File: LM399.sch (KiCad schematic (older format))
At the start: 8 parts, among them U1 LM399, U2 LTC2057

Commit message: Positive zener pin now has a sense connection to correct fot the error caused by the 1 mA zener current Changed zener bias current resistor to less expensive smd precision resistor Added a 2nd parallel resistor to the divider to make fine tuning easier Changed pin layout of the connector (due to the sense connection)
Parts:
- added R4: 34k, Custom_footprints:Vishay_S102K, symbol R
- added W1, W3: NET-TIE, Custom_footprints:NET-TIE-0.15mm, symbol NET-TIE
- added W2: NET-TIE, Custom_footprints:NET-TIE-0.20mm, symbol NET-TIE
- C1: Alternative (none) -> C1206C223J2GACAUTO; MFN Cornell Dubilier -> Kemet; MFP FCP1206H103J-H2 -> C1206C103JAGACTU; Note (none) -> Use *that* one!
- R1: value 3K -> 7.5K; footprint Custom_footprints:Vishay_S102 -> Resistors_SMD:R_0805; MFN Vishay -> Welwyn; MFP Y00623K00000B9L -> PCF0805-13-7K5-B-T1; Note TCR <= 5ppm, absolute precision unimportant -> (none)
- R2: value 9K -> 20k; footprint Custom_footprints:Vishay_S102 -> Custom_footprints:Vishay_S102K; MFP Y00629K00000T9L -> Y006220K0000T9L
- R3: value 20K -> 34k; footprint Custom_footprints:Vishay_S102 -> Custom_footprints:Vishay_S102K; MFP Y006220K0000T9L -> Y006234K0000T9L
- U1: MFP LM399A -> LM399AH
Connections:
- net labels added: V-heater+, V_heater-, V_zener+_force, V_zener+_sense
- wire segments 28 -> 37
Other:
- note added: "Information on insulation resistance can be found here:\nhttp://www.iequalscdvdt.com/Insulation_resis_.html\nhttps://www.vishay.com/docs/26033/gentechinfofilm.pdf"
- note added: "Kelvin connect the Zener. Even the the small current\npassing through R1 (1 mA) will introduce an error of 0.2 ppm/K\n(10 mm trace 0=> 0.2 ohm, 1 mA, 0.7 % tcr, ~~7 V reference)"
- note added: "Use a Film capacitor with a high insulation\nresistance (no polyester), which is stable\nover temperature. Nowadays C0G (BME) is\neven better than film."
- note added: "Use precision resistors\nwith an extremly low TCR\nor a network with very good\ntracking TCR."
- note added: "e.g. PCF0805-13-7K5-B-T1 (5 ppm),\nTE Connectivity RU73X2A7K5LTDF (2 ppm),\nVishay S102 (2 ppm)\n\nPCF0805-13-3K-B-T1. (5 ppm),\nVishay S102 (2 ppm)"
- note removed: "Use a Film capacitor with a high insulation\nresistance (no polyester), which is stable\nover temperature (PP, PPS)"
- note removed: "Use precision resistors\nwith an extremly low TCR\nor a network with very good\nTracking TCR."
- note removed: "e.g. PCF0805-13-7K5-B-T1 (5 ppm),\nTE Connectivity RU73X2A7K5LTDF (2 ppm),\nVishay S102 (2 ppm),\nor Vishay VSMP (0.05 ppm)\n\nPCF0805-13-3K-B-T1. (5 ppm),\nVishay S102 (2 ppm),\nor Vishay VSMP (0.05 ppm)"
- moved on the sheet: C1

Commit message: Reduced board size Changed voltage divider to Vishay 300144Z Removed guard ring Added startup resistor R5 Changed all capacitors to 100 nF C0G
Updated modules
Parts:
- removed R2: 20k, Custom_footprints:Vishay_S102K, symbol R
- removed R3, R4: 34k, Custom_footprints:Vishay_S102K, symbol R
- removed U2: LTC2057, Housings_SSOP:MSOP-10_3x3mm_Pitch0.5mm, symbol LTC2057(MSOP-10)
- added R5: 200k, Resistors_SMD:R_0603, symbol R
- added RN1: 17k/20k, Custom_footprints:Vishay_300144, symbol Voltage_Divider
- added U2: LTC2057, Housings_DFN_QFN:DFN-8-1EP_3x3mm_Pitch0.5mm, symbol LTC2057(DFN)
- C1: value 10n -> 100n; Alternative C1206C223J2GACAUTO -> (none); MFN Kemet -> Murata; MFP C1206C103JAGACTU -> GRM31C5C1H104JA01L; Note Use *that* one! -> (none)
- C2, C3: footprint Capacitors_SMD:C_0805 -> Capacitors_SMD:C_1206; MFN Cornell Dubilier -> Murata; MFP FCA0805C104M-J2 -> GRM31C5C1H104JA01L
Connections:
- wire segments 37 -> 33
- no-connect marks 3 -> 2
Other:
- note added: "Kelvin connect the Zener. Even the the small current\npassing through R1 (1 mA) will introduce an error of 0.2 ppm/K\ngiven a normal PCB copper trace.\n(10 mm trace 0=> 0.2 ohm, 1 mA, 0.7 % tcr, ~~7 V reference)"
- note added: "Mount the LM399 a *little* off the board,\nto keep stress away.\nSource: http://www.eevblog.com/forum/\nmetrology/ultra-precision-reference-ltz1000/\nmsg404500/#msg404500"
- note removed: "Guard ring"
- note removed: "Kelvin connect the Zener. Even the the small current\npassing through R1 (1 mA) will introduce an error of 0.2 ppm/K\n(10 mm trace 0=> 0.2 ohm, 1 mA, 0.7 % tcr, ~~7 V reference)"
- moved on the sheet: C1, C2, C3, R1, W2, W3

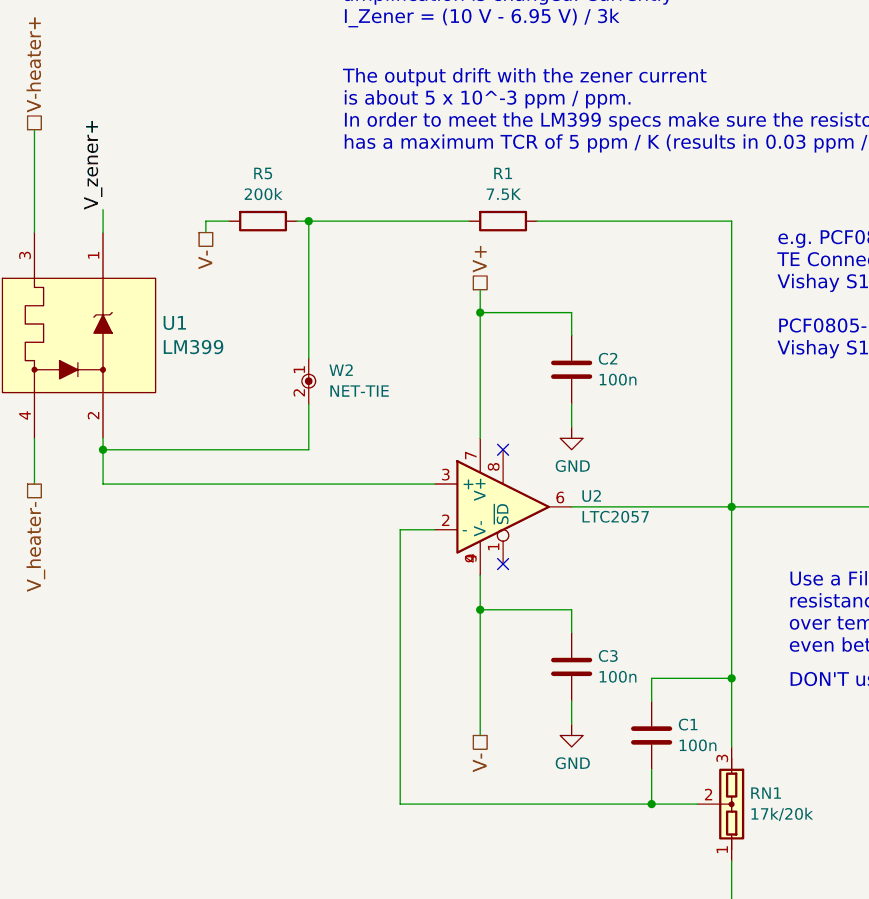
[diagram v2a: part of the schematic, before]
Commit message: Updated picture Updated annotations
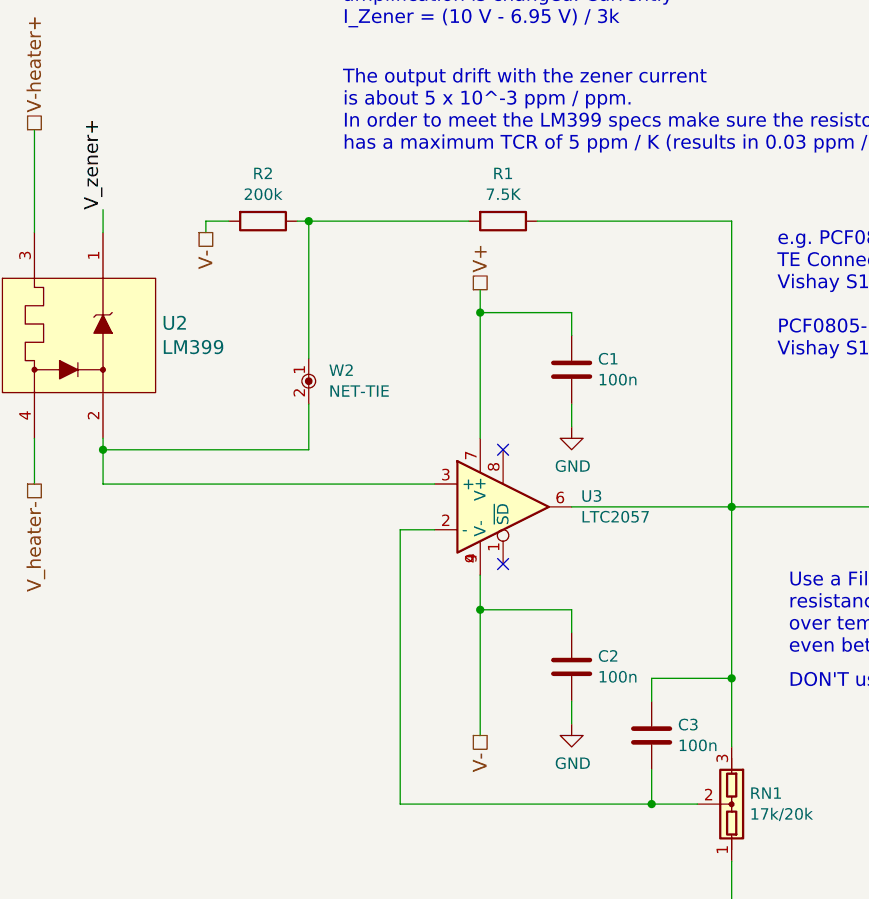
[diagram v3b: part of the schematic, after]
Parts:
- renumbered C2 to C1, C3 to C2, C1 to C3, R5 to R2, U1 to U2, U2 to U3
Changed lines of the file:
@@
 $EndDescr
 $Comp
-L LM399 U1
+L LM399 U2
 U 1 1 591A5398
 P 4000 3300
-F 0 "U1" H 4408 3353 60  0000 L CNN
+F 0 "U2" H 4408 3353 60  0000 L CNN
 F 1 "LM399" H 4408 3247 60  0000 L CNN
 F 2 "Custom_footprints:LM399" H 4000 3250 60  0001 C CNN
@@
 V_zener-
 $Comp
-L C C1
+L C C3
 U 1 1 591A53CC
 P 6550 5050
-F 0 "C1" H 6665 5096 50  0000 L CNN
+F 0 "C3" H 6665 5096 50  0000 L CNN
 F 1 "100n" H 6665 5005 50  0000 L CNN
 F 2 "Capacitors_SMD:C_1206" H 6588 4900 50  0001 C CNN
@@
 Use a Film capacitor with a high insulation\nresistance (no polyester), which is stable\nover temperature. Nowadays C0G (BME) is\neven better than film.
 $Comp
-L C C2
+L C C1
 U 1 1 591A5401
 P 6200 3450
-F 0 "C2" H 6315 3496 50  0000 L CNN
+F 0 "C1" H 6315 3496 50  0000 L CNN
 F 1 "100n" H 6315 3405 50  0000 L CNN
 F 2 "Capacitors_SMD:C_1206" H 6238 3300 50  0001 C CNN
@@
 $EndComp
 $Comp
-L GND #PWR05
+L GND #PWR2
 U 1 1 591A540B
 P 6200 3700
-F 0 "#PWR05" H 6200 3450 50  0001 C CNN
+F 0 "#PWR2" H 6200 3450 50  0001 C CNN
 F 1 "GND" H 6205 3527 50  0000 C CNN
 F 2 "" H 6200 3700 50  0001 C CNN
@@
 $EndComp
 $Comp
-L GND #PWR06
+L GND #PWR3
 U 1 1 591A5416
 P 6200 5000
-F 0 "#PWR06" H 6200 4750 50  0001 C CNN
+F 0 "#PWR3" H 6200 4750 50  0001 C CNN
 F 1 "GND" H 6205 4827 50  0000 C CNN
 F 2 "" H 6200 5000 50  0001 C CNN
@@
 $EndComp
 $Comp
-L C C3
+L C C2
 U 1 1 591A541E
 P 6200 4750
-F 0 "C3" H 6315 4796 50  0000 L CNN
+F 0 "C2" H 6315 4796 50  0000 L CNN
 F 1 "100n" H 6315 4705 50  0000 L CNN
 F 2 "Capacitors_SMD:C_1206" H 6238 4600 50  0001 C CNN
@@
 Information on insulation resistance can be found here:\nhttp://www.iequalscdvdt.com/Insulation_resis_.html\nhttps://www.vishay.com/docs/26033/gentechinfofilm.pdf
 $Comp
-L R R5
+L R R2
 U 1 1 59E8CFD2
 P 4850 2800
-F 0 "R5" V 4643 2800 50  0000 C CNN
+F 0 "R2" V 4643 2800 50  0000 C CNN
 F 1 "200k" V 4734 2800 50  0000 C CNN
 F 2 "Resistors_SMD:R_0603" V 4780 2800 50  0001 C CNN
@@
 	6900 5800 6900 5600
 $Comp
-L LTC2057(DFN) U2
+L LTC2057(DFN) U3
 U 1 1 5A502B7D
 P 5900 4050
-F 0 "U2" H 6241 4096 50  0000 L CNN
+F 0 "U3" H 6241 4096 50  0000 L CNN
 F 1 "LTC2057" H 6241 4005 50  0000 L CNN
 F 2 "Housings_DFN_QFN:DFN-8-1EP_3x3mm_Pitch0.5mm" H 6241 3959 50  0001 L CNN

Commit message: Updated schematic to KiCAD v5 Reduced board size even further by replacing the AD590 with a TMP236
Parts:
- C1, C2, C3: footprint Capacitors_SMD:C_1206 -> Capacitor_SMD:C_1206_3216Metric; symbol C -> Device:C
- NT1: renamed from W1; symbol NET-TIE -> Device:Net-Tie_2
- NT2: renamed from W2; symbol NET-TIE -> Device:Net-Tie_2
- NT3: renamed from W3; symbol NET-TIE -> Device:Net-Tie_2
- R1: footprint Resistors_SMD:R_0805 -> Resistor_SMD:R_0603_1608Metric; symbol R -> Device:R
- R2: footprint Resistors_SMD:R_0603 -> Resistor_SMD:R_0603_1608Metric; symbol R -> Device:R
- RN1: symbol Voltage_Divider -> Device:Voltage_Divider
- U2: symbol LM399 -> Linear-Technology:LM399
- U3: footprint Housings_DFN_QFN:DFN-8-1EP_3x3mm_Pitch0.5mm -> Package_DFN_QFN:DFN-8-1EP_3x3mm_P0.5mm_EP1.66x2.38mm; symbol LTC2057(DFN) -> Linear-Technology:LTC2057(DFN)
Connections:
- wire segments 33 -> 41
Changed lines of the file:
@@
-EESchema Schematic File Version 2
-LIBS:power
-LIBS:device
-LIBS:transistors
-LIBS:conn
-LIBS:linear
-LIBS:regul
-LIBS:74xx
-LIBS:cmos4000
-LIBS:adc-dac
-LIBS:memory
-LIBS:xilinx
-LIBS:microcontrollers
-LIBS:dsp
-LIBS:microchip
-LIBS:analog_switches
-LIBS:motorola
-LIBS:texas
-LIBS:intel
-LIBS:audio
-LIBS:interface
-LIBS:digital-audio
-LIBS:philips
-LIBS:display
-LIBS:cypress
-LIBS:siliconi
-LIBS:opto
-LIBS:atmel
-LIBS:contrib
-LIBS:valves
-LIBS:Linear Technology
-LIBS:ADI
-LIBS:net-tie
+EESchema Schematic File Version 4
 LIBS:reference_board-cache
 EELAYER 26 0
@@
 Sheet 2 2
 Title "LM399 negative voltage reference"
-Date "2018-01-06"
-Rev "v2.1.0"
+Date "2018-08-17"
+Rev "v2.2.0"
 Comp ""
 Comment1 "Copyright (©) 2018, Patrick Baus <patrick.baus@physik.tu-darmstadt.de>"
@@
 $EndDescr
 $Comp
-L LM399 U2
+L Linear-Technology:LM399 U2
 U 1 1 591A5398
 P 4000 3300
@@
 Use precision resistors\nwith an extremly low TCR\nor a network with very good\ntracking TCR.
 $Comp
-L R R1
+L Device:R R1
 U 1 1 591A53BD
 P 5900 2800
 F 0 "R1" V 5693 2800 50  0000 C CNN
 F 1 "7.5K" V 5784 2800 50  0000 C CNN
-F 2 "Resistors_SMD:R_0805" V 5830 2800 50  0001 C CNN
+F 2 "Resistor_SMD:R_0603_1608Metric" V 5830 2800 50  0001 C CNN
 F 3 "" H 5900 2800 50  0001 C CNN
 F 4 "Welwyn" H 5900 2800 60  0001 C CNN "MFN"
@@
 V_zener-
 $Comp
-L C C3
+L Device:C C3
 U 1 1 591A53CC
 P 6550 5050
 F 0 "C3" H 6665 5096 50  0000 L CNN
 F 1 "100n" H 6665 5005 50  0000 L CNN
-F 2 "Capacitors_SMD:C_1206" H 6588 4900 50  0001 C CNN
+F 2 "Capacitor_SMD:C_1206_3216Metric" H 6588 4900 50  0001 C CNN
 F 3 "" H 6550 5050 50  0001 C CNN
 F 4 "Murata" H 6550 5050 60  0001 C CNN "MFN"
@@
 Use a Film capacitor with a high insulation\nresistance (no polyester), which is stable\nover temperature. Nowadays C0G (BME) is\neven better than film.
 $Comp
-L C C1
+L Device:C C1
 U 1 1 591A5401
 P 6200 3450
 F 0 "C1" H 6315 3496 50  0000 L CNN
 F 1 "100n" H 6315 3405 50  0000 L CNN
-F 2 "Capacitors_SMD:C_1206" H 6238 3300 50  0001 C CNN
+F 2 "Capacitor_SMD:C_1206_3216Metric" H 6238 3300 50  0001 C CNN
 F 3 "" H 6200 3450 50  0001 C CNN
 F 4 "Murata" H 6200 3450 60  0001 C CNN "MFN"
@@
 $EndComp
 $Comp
-L GND #PWR2
+L power:GND #PWR02
 U 1 1 591A540B
 P 6200 3700
-F 0 "#PWR2" H 6200 3450 50  0001 C CNN
+F 0 "#PWR02" H 6200 3450 50  0001 C CNN
 F 1 "GND" H 6205 3527 50  0000 C CNN
 F 2 "" H 6200 3700 50  0001 C CNN
@@
 $EndComp
 $Comp
-L GND #PWR3
+L power:GND #PWR03
 U 1 1 591A5416
 P 6200 5000
-F 0 "#PWR3" H 6200 4750 50  0001 C CNN
+F 0 "#PWR03" H 6200 4750 50  0001 C CNN
 F 1 "GND" H 6205 4827 50  0000 C CNN
 F 2 "" H 6200 5000 50  0001 C CNN
@@
 $EndComp
 $Comp
-L C C2
+L Device:C C2
 U 1 1 591A541E
 P 6200 4750
 F 0 "C2" H 6315 4796 50  0000 L CNN
 F 1 "100n" H 6315 4705 50  0000 L CNN
-F 2 "Capacitors_SMD:C_1206" H 6238 4600 50  0001 C CNN
+F 2 "Capacitor_SMD:C_1206_3216Metric" H 6238 4600 50  0001 C CNN
 F 3 "" H 6200 4750 50  0001 C CNN
 F 4 "Murata" H 6200 4750 60  0001 C CNN "MFN"
@@
 V_zener+_sense
 $Comp
-L NET-TIE W1
+L Device:Net-Tie_2 NT1
 U 1 1 5976DF85
 P 2800 2650
-F 0 "W1" V 2754 2738 50  0000 L CNN
+F 0 "NT1" V 2754 2738 50  0000 L CNN
 F 1 "NET-TIE" V 2845 2738 50  0000 L CNN
 F 2 "Custom_footprints:NET-TIE-0.15mm" H 2800 2550 50  0001 C CNN
@@
 $EndComp
 $Comp
-L NET-TIE W3
+L Device:Net-Tie_2 NT3
 U 1 1 5976E542
 P 6900 5900
-F 0 "W3" V 6854 5988 50  0000 L CNN
+F 0 "NT3" V 6854 5988 50  0000 L CNN
 F 1 "NET-TIE" V 6945 5988 50  0000 L CNN
 F 2 "Custom_footprints:NET-TIE-0.15mm" H 6900 5800 50  0001 C CNN
@@
 V_zener+
 $Comp
-L NET-TIE W2
+L Device:Net-Tie_2 NT2
 U 1 1 5976EB13
 P 5050 3500
-F 0 "W2" V 5004 3588 50  0000 L CNN
+F 0 "NT2" V 5004 3588 50  0000 L CNN
 F 1 "NET-TIE" V 5095 3588 50  0000 L CNN
 F 2 "Custom_footprints:NET-TIE-0.20mm" H 5050 3400 50  0001 C CNN
@@
 Information on insulation resistance can be found here:\nhttp://www.iequalscdvdt.com/Insulation_resis_.html\nhttps://www.vishay.com/docs/26033/gentechinfofilm.pdf
 $Comp
-L R R2
+L Device:R R2
 U 1 1 59E8CFD2
 P 4850 2800
 F 0 "R2" V 4643 2800 50  0000 C CNN
 F 1 "200k" V 4734 2800 50  0000 C CNN
-F 2 "Resistors_SMD:R_0603" V 4780 2800 50  0001 C CNN
+F 2 "Resistor_SMD:R_0603_1608Metric" V 4780 2800 50  0001 C CNN
 F 3 "" H 4850 2800 50  0001 C CNN
 F 4 "Susumu" H 4850 2800 60  0001 C CNN "MFN"
@@
 	2500 2500 2500 2950
 Wire Wire Line
-	6900 2800 6900 5100
-Wire Wire Line
-	6200 4050 7550 4050
+	6900 2800 6900 4050
+Wire Wire Line
+	6200 4050 6900 4050
 Wire Wire Line
 	5450 4150 5600 4150
@@
 	4150 3950 5600 3950
 Wire Wire Line
-	5000 2800 5750 2800
+	5000 2800 5050 2800
 Wire Wire Line
 	6050 2800 6900 2800
 Connection ~ 6900 4050
 Wire Wire Line
-	5800 4350 5800 5050
-Wire Wire Line
-	5800 3100 5800 3750
+	5800 4350 5800 4500
+Wire Wire Line
+	5800 3100 5800 3200
 Connection ~ 6900 4800
 Wire Wire Line
@@
 Connection ~ 5800 4500
 Wire Wire Line
-	4150 3750 4150 3950
+	4150 3750 4150 3800
 Wire Wire Line
 	2500 2950 2800 2750
@@
 Mount the LM399 a *little* off the board,\nto keep stress away.\nSource: http://www.eevblog.com/forum/\nmetrology/ultra-precision-reference-ltz1000/\nmsg404500/#msg404500
 $Comp
-L Voltage_Divider RN1
+L Device:Voltage_Divider RN1
 U 1 1 5A502407
 P 6900 5350
@@
 $EndComp
 Wire Wire Line
-	5450 5350 6750 5350
+	5450 5350 6550 5350
 Wire Wire Line
 	6900 5800 6900 5600
 $Comp
-L LTC2057(DFN) U3
+L Linear-Technology:LTC2057(DFN) U3
 U 1 1 5A502B7D
 P 5900 4050
 F 0 "U3" H 6241 4096 50  0000 L CNN
 F 1 "LTC2057" H 6241 4005 50  0000 L CNN
-F 2 "Housings_DFN_QFN:DFN-8-1EP_3x3mm_Pitch0.5mm" H 6241 3959 50  0001 L CNN
+F 2 "Package_DFN_QFN:DFN-8-1EP_3x3mm_P0.5mm_EP1.66x2.38mm" H 6241 3959 50  0001 L CNN
 F 3 "" H 5950 4250 50  0000 C CNN
 F 4 "Linear Technology" H 6500 4350 60  0001 C CNN "MFN"
@@
 Wire Wire Line
 	5450 4150 5450 5350
+Wire Wire Line
+	5050 2800 5750 2800
+Wire Wire Line
+	6900 4050 6900 4800
+Wire Wire Line
+	6900 4050 7550 4050
+Wire Wire Line
+	6900 4800 6900 5100
+Wire Wire Line
+	5800 3200 5800 3750
+Wire Wire Line
+	5800 4500 5800 5050
+Wire Wire Line
+	4150 3800 4150 3950
+Wire Wire Line
+	6550 5350 6750 5350
 $EndSCHEMATC

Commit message: Updated component datasheets
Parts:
- RN1: MFP 300144ZT -> 300144Z
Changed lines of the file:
@@
 F 3 "" H 7100 5350 50  0001 C CNN
 F 4 "Vishay" H 6900 5350 60  0001 C CNN "MFN"
-F 5 "300144ZT" H 6900 5350 60  0001 C CNN "MFP"
+F 5 "300144Z" H 6900 5350 60  0001 C CNN "MFP"
 	1    6900 5350
 	-1   0    0    1

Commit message: Update to version 3.0 (compatible with the current driver RC2) Replaced the chopper amplifier with the LT1001 Updated the libraries
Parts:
- removed U3: LTC2057, Package_DFN_QFN:DFN-8-1EP_3x3mm_P0.5mm_EP1.66x2.38mm, symbol Linear-Technology:LTC2057(DFN)
- added NT4, NT5: NET-TIE, Custom_footprints:NET-TIE-0.20mm, symbol Device:Net-Tie_2
- added U3: LT1001, Package_SO:SOIC-8_3.9x4.9mm_P1.27mm, symbol Amplifier_Operational:LT1363
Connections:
- wire segments 41 -> 43
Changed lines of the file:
@@
 Sheet 2 2
 Title "LM399 negative voltage reference"
-Date "2018-08-17"
+Date "2018-10-04"
 Rev "v3.0.0"
 Comp ""
@@
 Text Notes 1850 4000 0    60   ~ 0
 TODO:\n- use 4 drill holes to mount styrofoam
-Text Notes 7150 4700 0    60   ~ 0
+Text Notes 7350 4900 0    60   ~ 0
 Use a Film capacitor with a high insulation\nresistance (no polyester), which is stable\nover temperature. Nowadays C0G (BME) is\neven better than film.
 $Comp
@@
 Text Notes 7100 3400 0    60   ~ 0
 e.g. PCF0805-13-7K5-B-T1 (5 ppm),\nTE Connectivity RU73X2A7K5LTDF (2 ppm),\nVishay S102 (2 ppm)\n\nPCF0805-13-3K-B-T1. (5 ppm),\nVishay S102 (2 ppm)
-Text Notes 7150 4850 0    60   ~ 0
+Text Notes 7350 5050 0    60   ~ 0
 DON'T use AVX! They will melt at the spec'ed temperature
 Text Notes 4300 6300 0    60   ~ 0
@@
 Text Notes 3200 1650 0    60   ~ 0
 Trace resistance of 0.32 Ohm\n(100mm, 4000 ppm / K) causes\na 1.5 µV / K error.
-NoConn ~ 5900 3800
-NoConn ~ 5900 4300
+NoConn ~ 6000 4350
+NoConn ~ 5900 4350
 Text HLabel 2800 2500 1    60   Output ~ 0
 V_zener+_sense
@@
 	2500 2500 2500 2950
 Wire Wire Line
-	6900 2800 6900 4050
-Wire Wire Line
 	6200 4050 6900 4050
 Wire Wire Line
@@
 Wire Wire Line
 	5800 3100 5800 3200
-Connection ~ 6900 4800
 Wire Wire Line
 	5800 3200 6200 3200
@@
 Wire Wire Line
 	6900 5800 6900 5600
-$Comp
-L Linear-Technology:LTC2057(DFN) U3
-U 1 1 5A502B7D
+Wire Wire Line
+	5450 4150 5450 5350
+Wire Wire Line
+	5050 2800 5750 2800
+Wire Wire Line
+	6900 4050 7550 4050
+Wire Wire Line
+	6900 4800 6900 5100
+Wire Wire Line
+	5800 3200 5800 3750
+Wire Wire Line
+	5800 4500 5800 5050
+Wire Wire Line
+	4150 3800 4150 3950
+Wire Wire Line
+	6550 5350 6750 5350
+$Comp
+L Amplifier_Operational:LT1363 U3
+U 1 1 5BB4F780
 P 5900 4050
-F 0 "U3" H 6241 4096 50  0000 L CNN
-F 1 "LTC2057" H 6241 4005 50  0000 L CNN
-F 2 "Package_DFN_QFN:DFN-8-1EP_3x3mm_P0.5mm_EP1.66x2.38mm" H 6241 3959 50  0001 L CNN
-F 3 "" H 5950 4250 50  0000 C CNN
-F 4 "Linear Technology" H 6500 4350 60  0001 C CNN "MFN"
-F 5 "LTC2057IDD" H 6300 4450 60  0001 C CNN "MFP"
+F 0 "U3" H 6250 4100 50  0000 L CNN
+F 1 "LT1001" H 6250 4000 50  0000 L CNN
+F 2 "Package_SO:SOIC-8_3.9x4.9mm_P1.27mm" H 5950 4100 50  0001 C CNN
+F 3 "http://www.analog.com/media/en/technical-documentation/data-sheets/1001fb.pdf" H 5950 4200 50  0001 C CNN
+F 4 "Analog Devices" H 5900 4050 50  0001 C CNN "MFN"
+F 5 "LT1001CS8" H 5900 4050 50  0001 C CNN "MFP"
 	1    5900 4050
 	1    0    0    -1
 $EndComp
-Wire Wire Line
-	5450 4150 5450 5350
-Wire Wire Line
-	5050 2800 5750 2800
-Wire Wire Line
-	6900 4050 6900 4800
-Wire Wire Line
-	6900 4050 7550 4050
-Wire Wire Line
-	6900 4800 6900 5100
-Wire Wire Line
-	5800 3200 5800 3750
-Wire Wire Line
-	5800 4500 5800 5050
-Wire Wire Line
-	4150 3800 4150 3950
-Wire Wire Line
-	6550 5350 6750 5350
+$Comp
+L Device:Net-Tie_2 NT4
+U 1 1 5BB5735D
+P 6900 3550
+F 0 "NT4" V 6854 3638 50  0000 L CNN
+F 1 "NET-TIE" V 6945 3638 50  0000 L CNN
+F 2 "Custom_footprints:NET-TIE-0.20mm" H 6900 3450 50  0001 C CNN
+F 3 "" H 6900 3550 60  0000 C CNN
+	1    6900 3550
+	0    1    1    0
+$EndComp
+Wire Wire Line
+	6900 2800 6900 3450
+Wire Wire Line
+	6900 3650 6900 4050
+$Comp
+L Device:Net-Tie_2 NT5
+U 1 1 5BB58169
+P 6900 4350
+F 0 "NT5" V 6854 4438 50  0000 L CNN
+F 1 "NET-TIE" V 6945 4438 50  0000 L CNN
+F 2 "Custom_footprints:NET-TIE-0.20mm" H 6900 4250 50  0001 C CNN
+F 3 "" H 6900 4350 60  0000 C CNN
+	1    6900 4350
+	0    1    1    0
+$EndComp
+Wire Wire Line
+	6900 4050 6900 4250
+Wire Wire Line
+	6900 4450 6900 4800
+Connection ~ 6900 4800
 $EndSCHEMATC
